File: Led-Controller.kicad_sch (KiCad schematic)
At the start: 42 parts, among them J1 Barrel_Jack_Switch_Pin3Ring, J2 Screw_Terminal_01x06, Q1 PMOS, Q2 PMOS, Q3 PMOS, Q4 PMOS, Q5 PMOS, U1 1ED44175N01BXTSA1, U2 1ED44175N01BXTSA1, U3 1ED44175N01BXTSA1, U4 1ED44175N01BXTSA1, U5 1ED44175N01BXTSA1, U6 ESP32-WROOM-32E, U7 AMS1117-3.3, U8 AMS1117-5.0

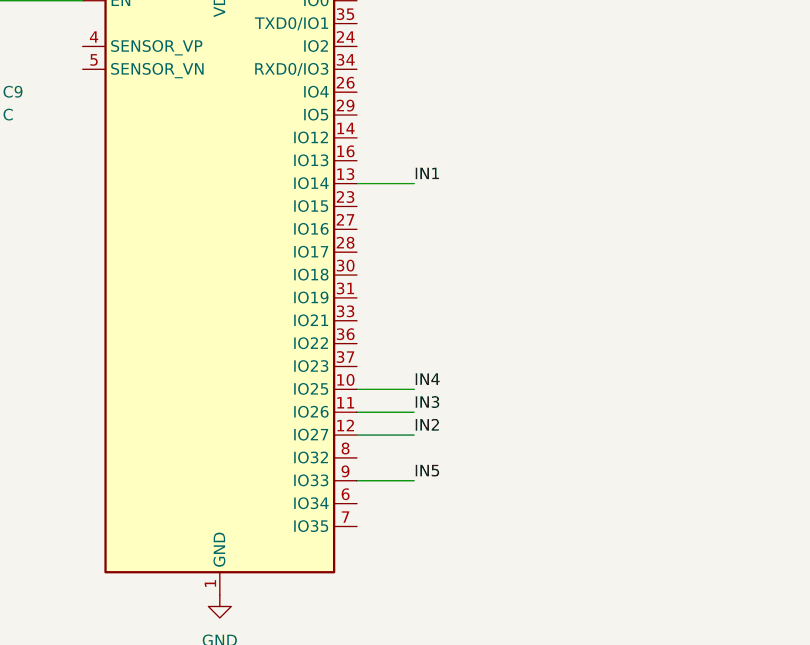
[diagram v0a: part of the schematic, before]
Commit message: Fixed: Pin assignment
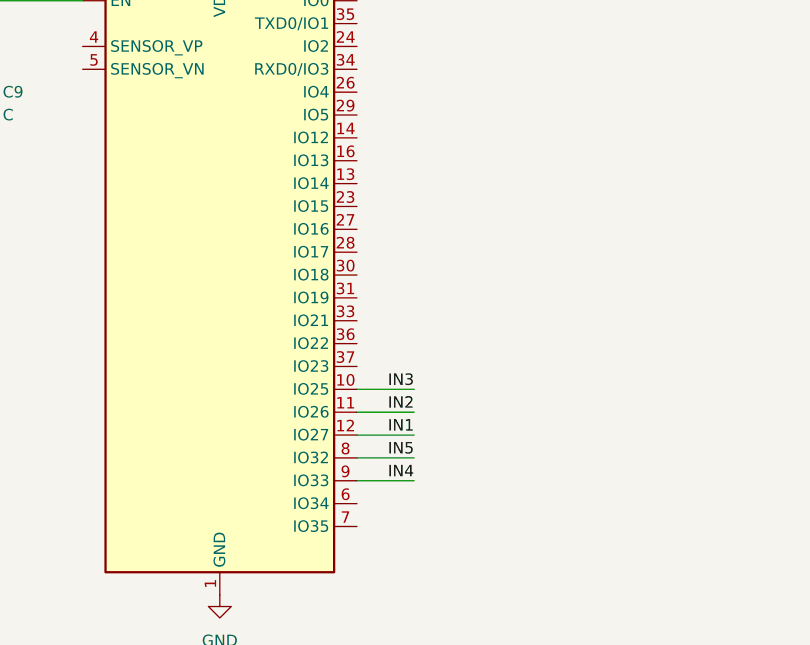
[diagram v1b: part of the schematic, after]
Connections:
- net IN1: now also U6.12 (IO27); no longer U6.13 (IO14)
- net IN2: now also U6.11 (IO26); no longer U6.12 (IO27)
- net IN3: now also U6.10 (IO25); no longer U6.11 (IO26)
- net IN4: now also U6.9 (IO33); no longer U6.10 (IO25)
- net IN5: now also U6.8 (IO32); no longer U6.9 (IO33)

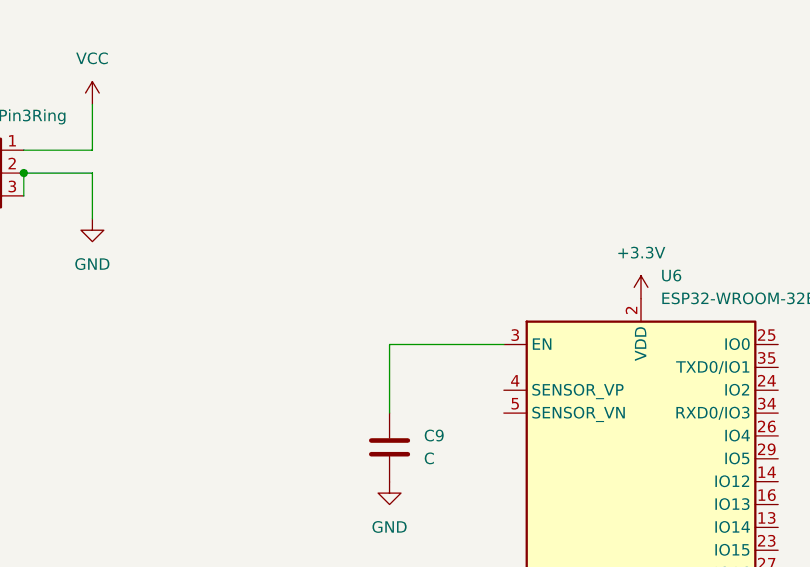
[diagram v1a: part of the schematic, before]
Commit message: Added: Pull up resistor for EN pin
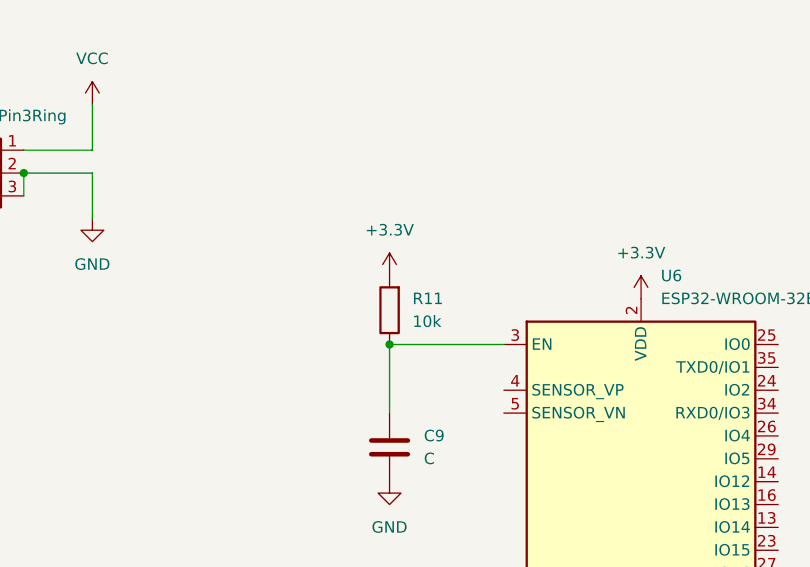
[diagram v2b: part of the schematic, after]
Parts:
- added R11: 10k, Resistor_SMD:R_0805_2012Metric_Pad1.20x1.40mm_HandSolder, symbol Device:R
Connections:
- net +3.3V: now also R11.2
- net at C9.1, U6.3 (EN): now also R11.1
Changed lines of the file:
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@@
 		(color 0 0 0 0)
 	)
+	(junction
+		(at 85.09 137.16)
+		(diameter 0)
+		(color 0 0 0 0)
+	)
 	(wire
 		(pts
@@
 	)
 	(symbol
+		(lib_id "Device:R")
+		(at 85.09 133.35 180)
+		(unit 1)
+		(exclude_from_sim no)
+		(in_bom yes)
+		(on_board yes)
+		(dnp no)
+		(fields_autoplaced yes)
+		(property "Reference" "R11"
+			(at 87.63 132.0799 0)
+			(effects
+				(font
+					(size 1.27 1.27)
+				)
+				(justify right)
+			)
+		)
+		(property "Value" "10k"
+			(at 87.63 134.6199 0)
+			(effects
+				(font
+					(size 1.27 1.27)
+				)
+				(justify right)
+			)
+		)
+		(property "Footprint" "Resistor_SMD:R_0805_2012Metric_Pad1.20x1.40mm_HandSolder"
+			(at 86.868 133.35 90)
+			(effects
+				(font
+					(size 1.27 1.27)
+				)
+				(hide yes)
+			)
+		)
+		(property "Datasheet" "~"
+			(at 85.09 133.35 0)
+			(effects
+				(font
+					(size 1.27 1.27)
+				)
+				(hide yes)
+			)
+		)
+		(property "Description" "Resistor"
+			(at 85.09 133.35 0)
+			(effects
+				(font
+					(size 1.27 1.27)
+				)
+				(hide yes)
+			)
+		)
+		(pin "2"
+		)
+		(pin "1"
+		)
+		(instances
+			(project "Led-Controller"
+				(path "/222b9972-7c70-4368-986f-3bb219717620"
+					(reference "R11")
+					(unit 1)
+				)
+			)
+		)
+	)
+	(symbol
 		(lib_id "power:GND")
 		(at 113.03 203.2 0)
@@
 					(unit 1)
 				)
+			)
+		)
+	)
+	(symbol
+		(lib_id "power:+3.3V")
+		(at 85.09 129.54 0)
+		(unit 1)
+		(exclude_from_sim no)
+		(in_bom yes)
+		(on_board yes)
+		(dnp no)
+		(fields_autoplaced yes)
+		(property "Reference" "#PWR069"
+			(at 85.09 133.35 0)
+			(effects
+				(font
+					(size 1.27 1.27)
+				)
+				(hide yes)
+			)
+		)
+		(property "Value" "+3.3V"
+			(at 85.09 124.46 0)
+			(effects
+				(font
+					(size 1.27 1.27)
+				)
+			)
+		)
+		(property "Footprint" ""
+			(at 85.09 129.54 0)
+			(effects
+				(font
+					(size 1.27 1.27)
+				)
+				(hide yes)
+			)
+		)
+		(property "Datasheet" ""
+			(at 85.09 129.54 0)
+			(effects
+				(font
+					(size 1.27 1.27)
+				)
+				(hide yes)
+			)
+		)
+		(property "Description" "Power symbol creates a global label with name \"+3.3V\""
+			(at 85.09 129.54 0)
+			(effects
+				(font
+					(size 1.27 1.27)
+				)
+				(hide yes)
+			)
+		)
+		(pin "1"
+		)
+		(instances
+			(project "Led-Controller"
+				(path "/222b9972-7c70-4368-986f-3bb219717620"
+					(reference "#PWR069")
+					(unit 1)
+				)

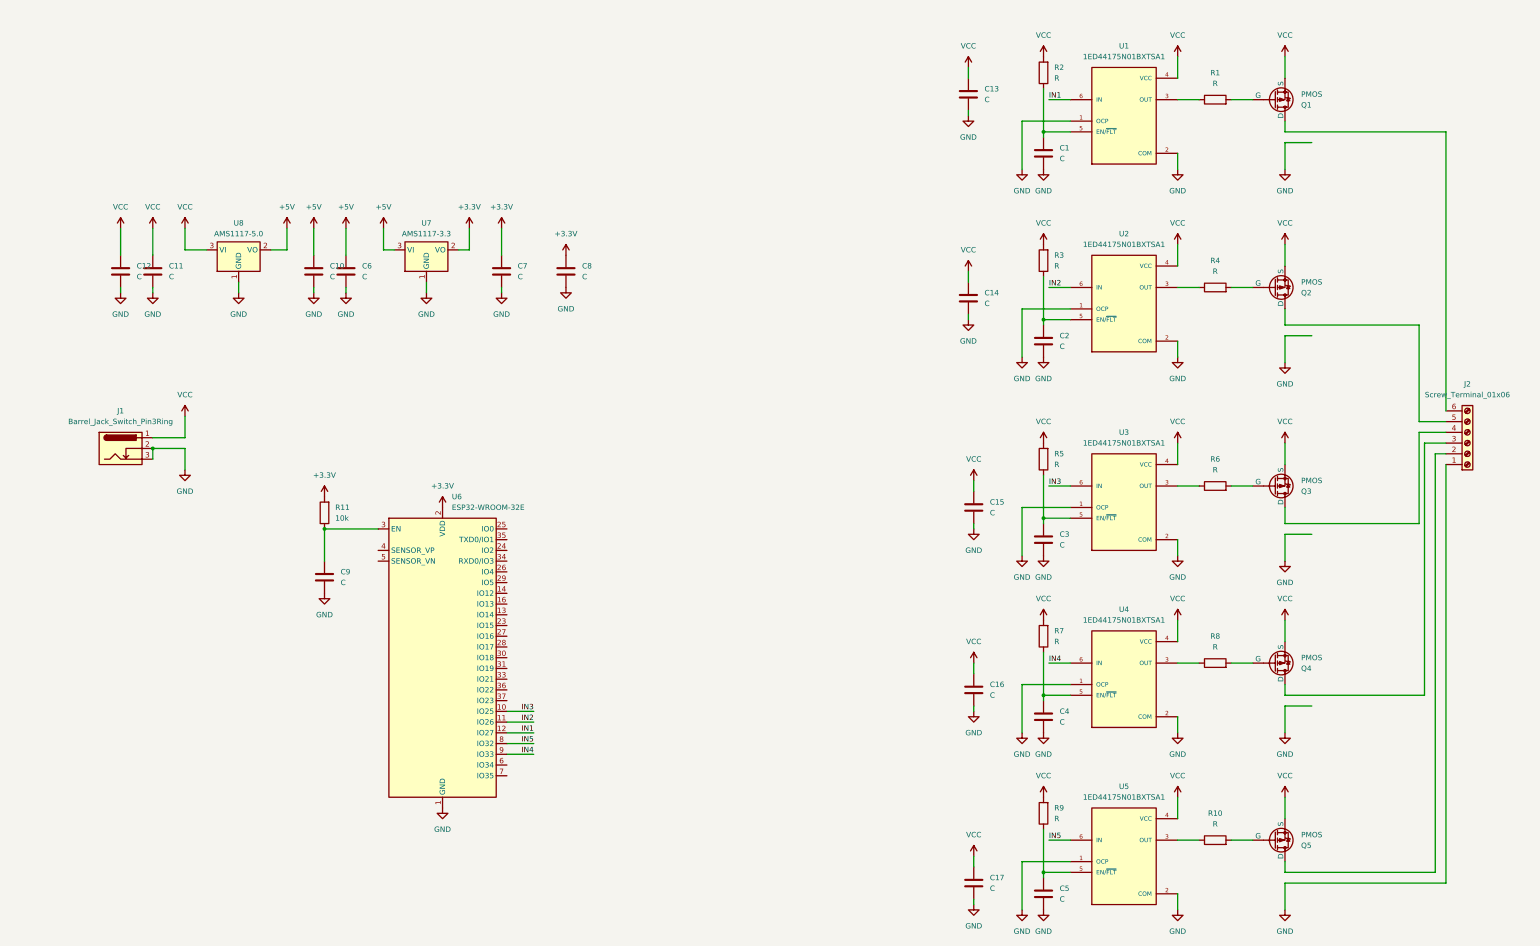
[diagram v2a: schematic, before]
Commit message: Added: N channel mosfet in place of P channel mosfet (#16)
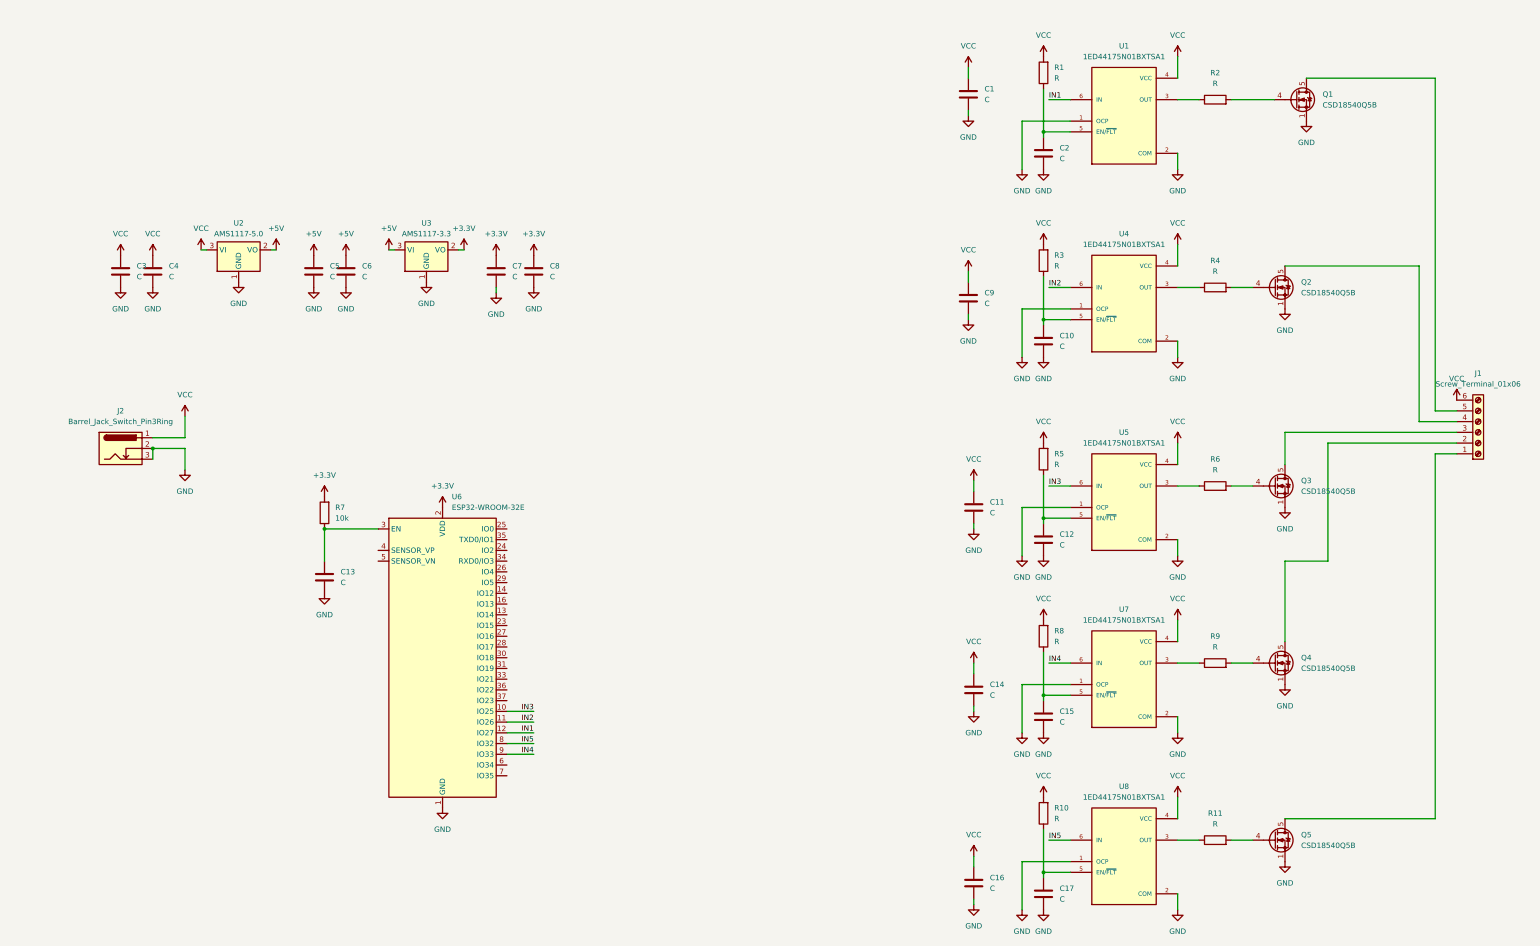
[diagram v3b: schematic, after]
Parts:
- removed Q1, Q2, Q3, Q4, Q5: PMOS, BSZ180P03:BSZ180P03, symbol Simulation_SPICE:PMOS
- added Q1, Q2, Q3, Q4, Q5: CSD18540Q5B, Package_TO_SOT_SMD:TDSON-8-1, symbol Transistor_FET:CSD18540Q5B
- renumbered C13 to C1, C2 to C10, C15 to C11, C3 to C12, C9 to C13, C16 to C14, C4 to C15, C17 to C16, C5 to C17, C1 to C2, C12 to C3, C11 to C4, C10 to C5, C14 to C9, J2 to J1, J1 to J2, R2 to R1, R9 to R10, R10 to R11, R1 to R2, R11 to R7, R7 to R8, R8 to R9, U8 to U2, U7 to U3, U2 to U4, U3 to U5, U4 to U7, U5 to U8
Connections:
- net GND: now also Q1.1 (S), Q1.2 (S), Q1.3 (S), Q2.1 (S), Q2.2 (S), Q2.3 (S), Q3.1 (S), Q3.2 (S), Q3.3 (S), Q4.1 (S), Q4.2 (S), Q4.3 (S), Q5.1 (S), Q5.2 (S), Q5.3 (S); no longer J1.1 (Pin_1)
- net VCC: now also J1.6 (Pin_6)
- net at J1.3 (Pin_3): now also Q3.5 (D)
- net at R9.2: now also Q4.4 (G)
- net at R4.2: now also Q2.4 (G)
- net at J1.2 (Pin_2): now also Q4.5 (D)
- net at J1.4 (Pin_4): now also Q2.5 (D)
- net at J1.5 (Pin_5): now also Q1.5 (D)
- net at R6.2: now also Q3.4 (G)
- net at R2.2: now also Q1.4 (G)
- net at R11.2: now also Q5.4 (G)
- new net: J1.1 (Pin_1), Q5.5 (D)
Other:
- moved on the sheet: C7, C8, J1

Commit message: Changed Components to smaller Footprint (#18)
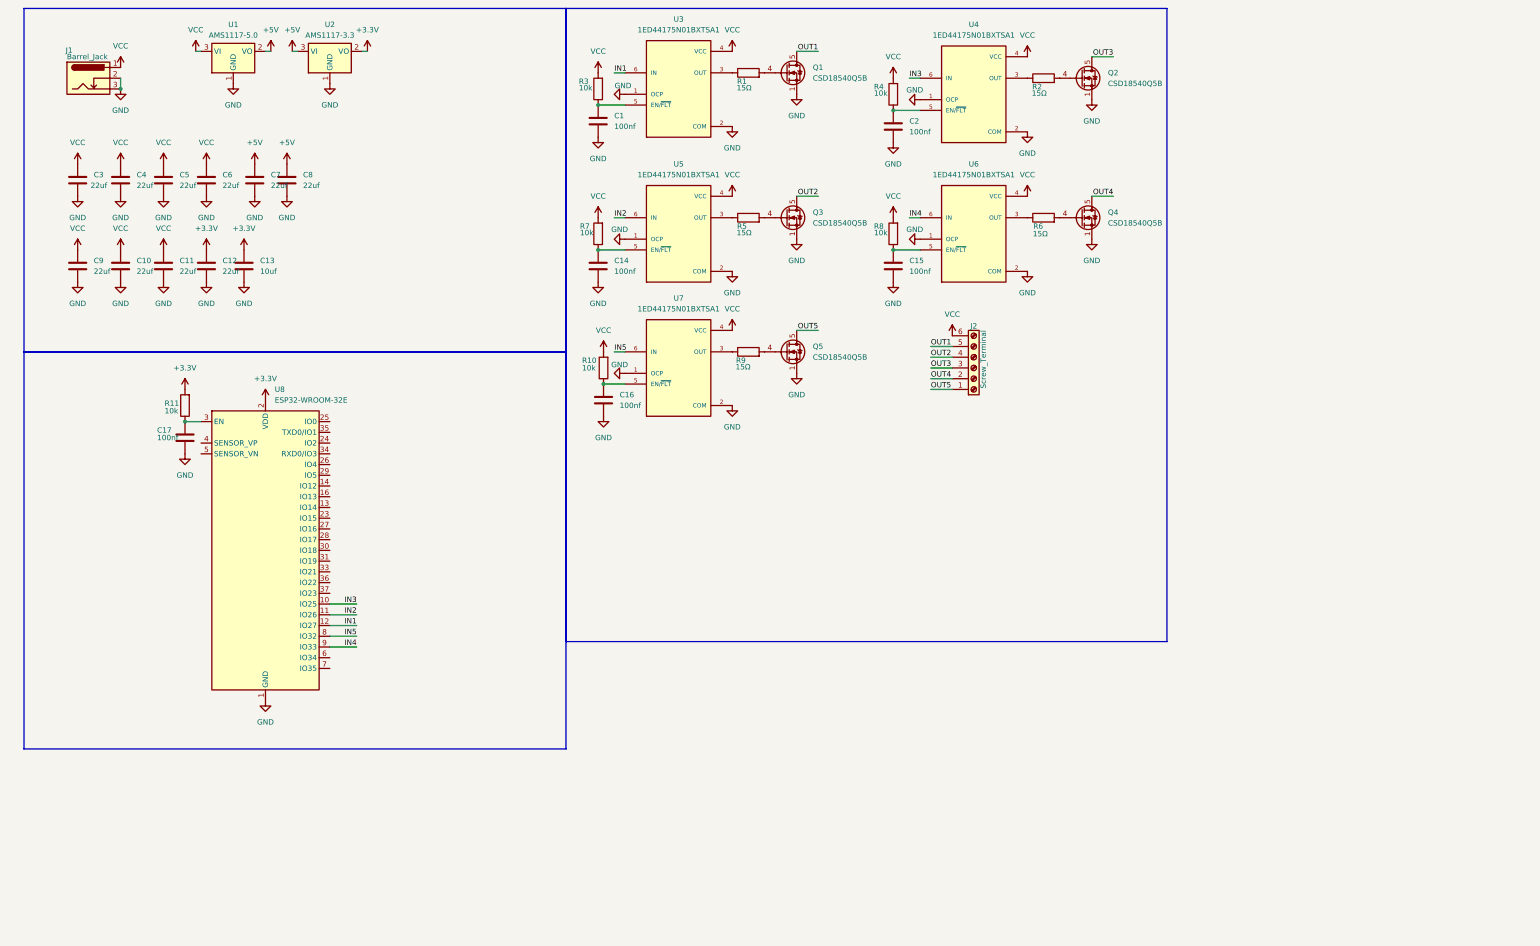
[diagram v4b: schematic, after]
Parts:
- C1: renamed from C2; value C -> 100nf; footprint Capacitor_SMD:C_0805_2012Metric_Pad1.18x1.45mm_HandSolder -> Capacitor_SMD:C_0402_1005Metric
- C10: renamed from C14; value C -> 22uf
- C11: renamed from C16; value C -> 22uf
- C12: renamed from C7; value C -> 22uf
- C13: renamed from C8; value C -> 10uf; footprint Capacitor_SMD:C_0805_2012Metric_Pad1.18x1.45mm_HandSolder -> Capacitor_SMD:C_0402_1005Metric
- C14: renamed from C10; value C -> 100nf; footprint Capacitor_SMD:C_0805_2012Metric_Pad1.18x1.45mm_HandSolder -> Capacitor_SMD:C_0402_1005Metric
- C15: value C -> 100nf; footprint Capacitor_SMD:C_0805_2012Metric_Pad1.18x1.45mm_HandSolder -> Capacitor_SMD:C_0402_1005Metric
- C16: renamed from C17; value C -> 100nf; footprint Capacitor_SMD:C_0805_2012Metric_Pad1.18x1.45mm_HandSolder -> Capacitor_SMD:C_0402_1005Metric
- C17: renamed from C13; value C -> 100nf; footprint Capacitor_SMD:C_0805_2012Metric_Pad1.18x1.45mm_HandSolder -> Capacitor_SMD:C_0402_1005Metric
- C2: renamed from C12; value C -> 100nf; footprint Capacitor_SMD:C_0805_2012Metric_Pad1.18x1.45mm_HandSolder -> Capacitor_SMD:C_0402_1005Metric
- C3: renamed from C9; value C -> 22uf
- C4: renamed from C1; value C -> 22uf
- C5: renamed from C3; value C -> 22uf
- C6: renamed from C4; value C -> 22uf
- C7: renamed from C5; value C -> 22uf
- C8: renamed from C6; value C -> 22uf
- C9: renamed from C11; value C -> 22uf
- J1: renamed from J2; value Barrel_Jack_Switch_Pin3Ring -> Barrel_Jack
- J2: renamed from J1; value Screw_Terminal_01x06 -> Screw_Terminal
- R1: renamed from R2; value R -> 15Ω; footprint Resistor_SMD:R_0805_2012Metric_Pad1.20x1.40mm_HandSolder -> Resistor_SMD:R_0402_1005Metric
- R10, R8: value R -> 10k; footprint Resistor_SMD:R_0805_2012Metric_Pad1.20x1.40mm_HandSolder -> Resistor_SMD:R_0402_1005Metric
- R11: renamed from R7; footprint Resistor_SMD:R_0805_2012Metric_Pad1.20x1.40mm_HandSolder -> Resistor_SMD:R_0402_1005Metric
- R2: renamed from R6; value R -> 15Ω; footprint Resistor_SMD:R_0805_2012Metric_Pad1.20x1.40mm_HandSolder -> Resistor_SMD:R_0402_1005Metric
- R3: renamed from R1; value R -> 10k; footprint Resistor_SMD:R_0805_2012Metric_Pad1.20x1.40mm_HandSolder -> Resistor_SMD:R_0402_1005Metric
- R4: renamed from R5; value R -> 10k; footprint Resistor_SMD:R_0805_2012Metric_Pad1.20x1.40mm_HandSolder -> Resistor_SMD:R_0402_1005Metric
- R5: renamed from R4; value R -> 15Ω; footprint Resistor_SMD:R_0805_2012Metric_Pad1.20x1.40mm_HandSolder -> Resistor_SMD:R_0402_1005Metric
- R6: renamed from R9; value R -> 15Ω; footprint Resistor_SMD:R_0805_2012Metric_Pad1.20x1.40mm_HandSolder -> Resistor_SMD:R_0402_1005Metric
- R7: renamed from R3; value R -> 10k; footprint Resistor_SMD:R_0805_2012Metric_Pad1.20x1.40mm_HandSolder -> Resistor_SMD:R_0402_1005Metric
- R9: renamed from R11; value R -> 15Ω; footprint Resistor_SMD:R_0805_2012Metric_Pad1.20x1.40mm_HandSolder -> Resistor_SMD:R_0402_1005Metric
- renumbered Q3 to Q2, Q2 to Q3, U2 to U1, U3 to U2, U1 to U3, U5 to U4, U4 to U5, U7 to U6, U8 to U7, U6 to U8
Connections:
- net OUT5: now reaches J2.1 (Pin_1), Q5.5 (D)
- net OUT4: now reaches J2.2 (Pin_2), Q4.5 (D)
- net OUT3: now reaches J2.3 (Pin_3), Q2.5 (D)
- net OUT2: now reaches J2.4 (Pin_4), Q3.5 (D)
- net OUT1: now reaches J2.5 (Pin_5), Q1.5 (D)
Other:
- moved on the sheet: C1, C10, C11, C12, C13, C14, C15, C16, C17, C2, C3, C4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
